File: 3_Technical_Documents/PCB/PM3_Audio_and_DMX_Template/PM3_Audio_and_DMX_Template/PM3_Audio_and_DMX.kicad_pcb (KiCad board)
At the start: 4 copper layers, 66 x 121.9 mm, 187 parts, among them J1 DMX-out, J2 LINE_IN, J3 HEADPHONE_JACK, J4 LINE_OUT, P1 Conn_02x32_Odd_Even, P2 Conn_02x32_Odd_Even, SW2 SW_DPDT_x2, SW3 SW_DPDT_x2, U1 ESP32-WROOM-32E, U10 CS4271, U11 OPA2134, U12 OPA2134, U13 OPA2134, U14 TPA6110A2DGN, U2 LT3045xMSE, U3 6N136S, U4 CRE1S0505SC, U5 ST485E, U6 OPA322, U7 TLV61070ADBV, U8 LD3985M33R_SOT23, U8 LT3045xMSE, U9 LT3045xMSE

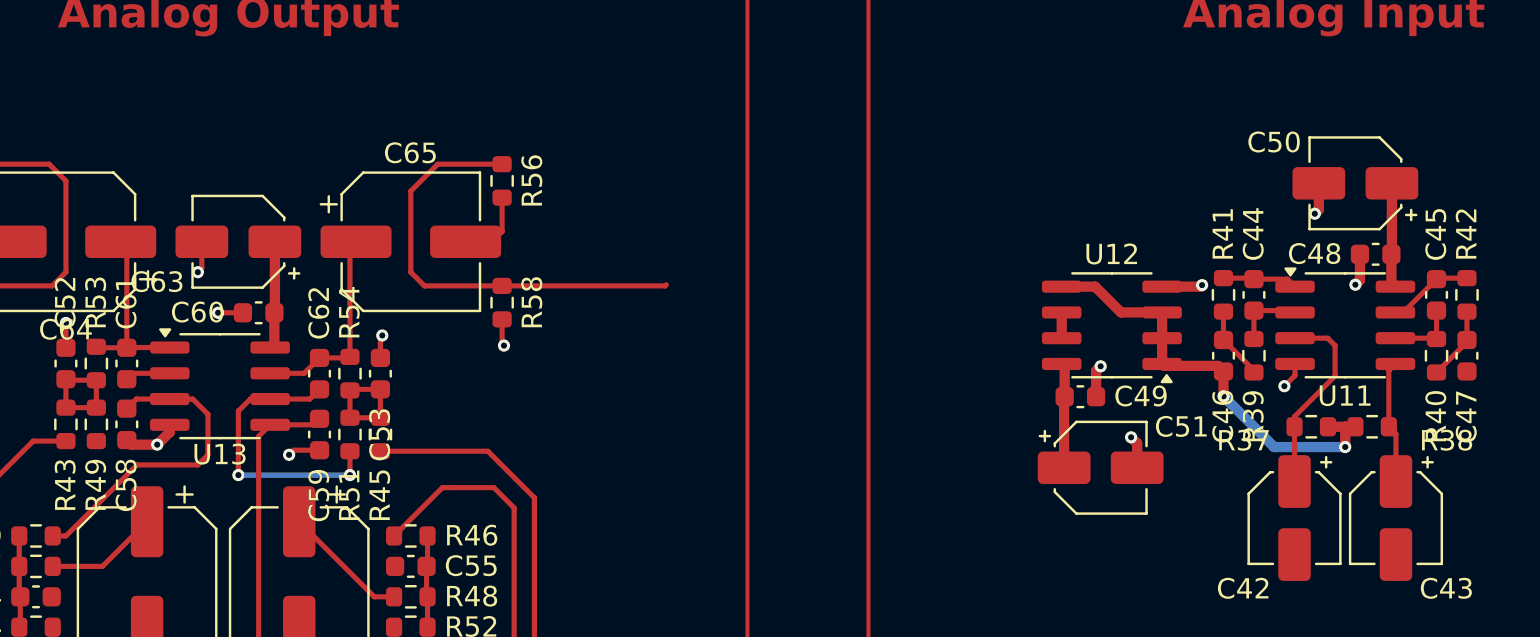
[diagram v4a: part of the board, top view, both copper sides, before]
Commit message: updated capacitors
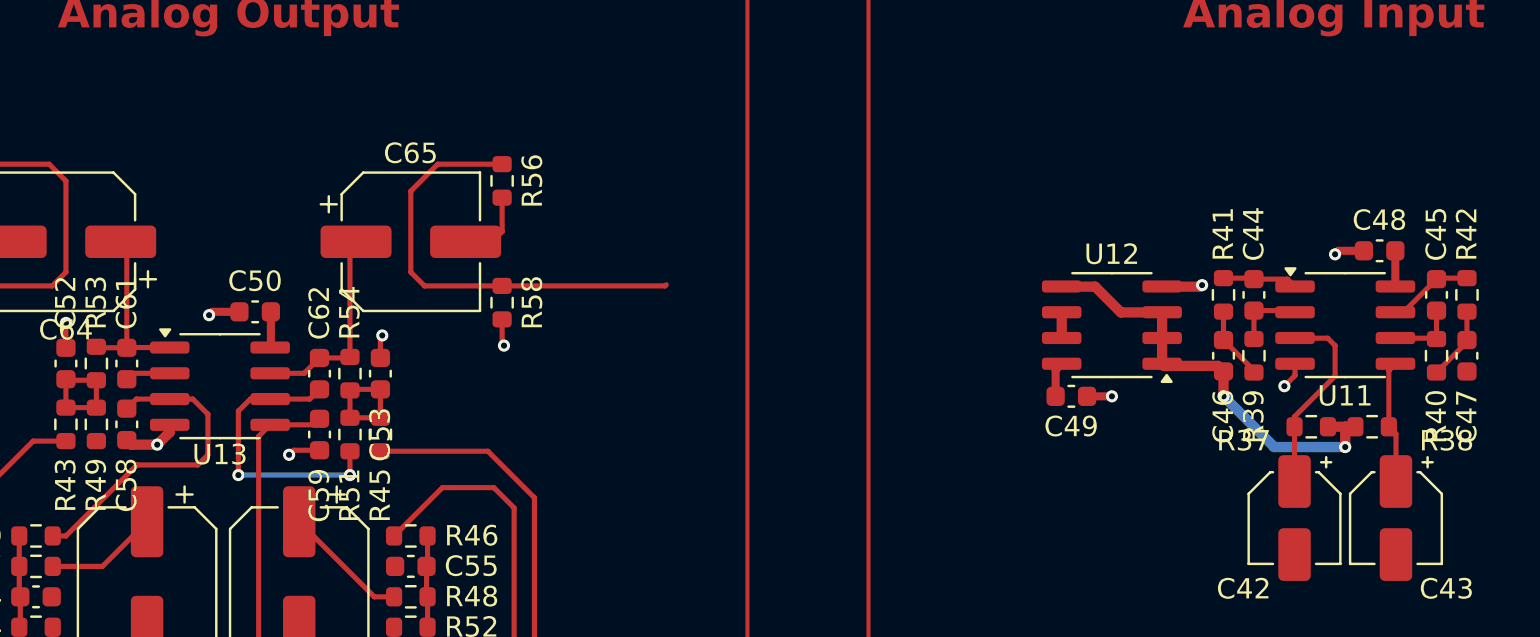
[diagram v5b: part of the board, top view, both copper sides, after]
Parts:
- removed C51, C63: 1u ELEC, Capacitor_SMD:CP_Elec_4x5.8
- removed C60: 10n COG/X7R, Capacitor_SMD:C_0603_1608Metric
- C48, C49: value 10n COG/X7R -> 100n
- C50: value 1u ELEC -> 100n; footprint Capacitor_SMD:CP_Elec_4x5.8 -> Capacitor_SMD:C_0603_1608Metric
- moved C50 54.6 mm to (114.8, -32.7)
- moved C49 0.45 mm to (155.0, -28.5)
- moved C48 0.26 mm to (170.2, -35.7)
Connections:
- R1 pad 2: Net-(U1-IO17) -> Net-(U1-IO16)
- U1 pad 27: unconnected-(U1-IO16-Pad27) -> Net-(U1-IO16)
- U1 pad 28: Net-(U1-IO17) -> unconnected-(U1-IO17-Pad28)
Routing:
- net VA: track 48.2 -> 37.8 mm
- net GND: track 92.5 -> 87.6 mm, vias 85 -> 82

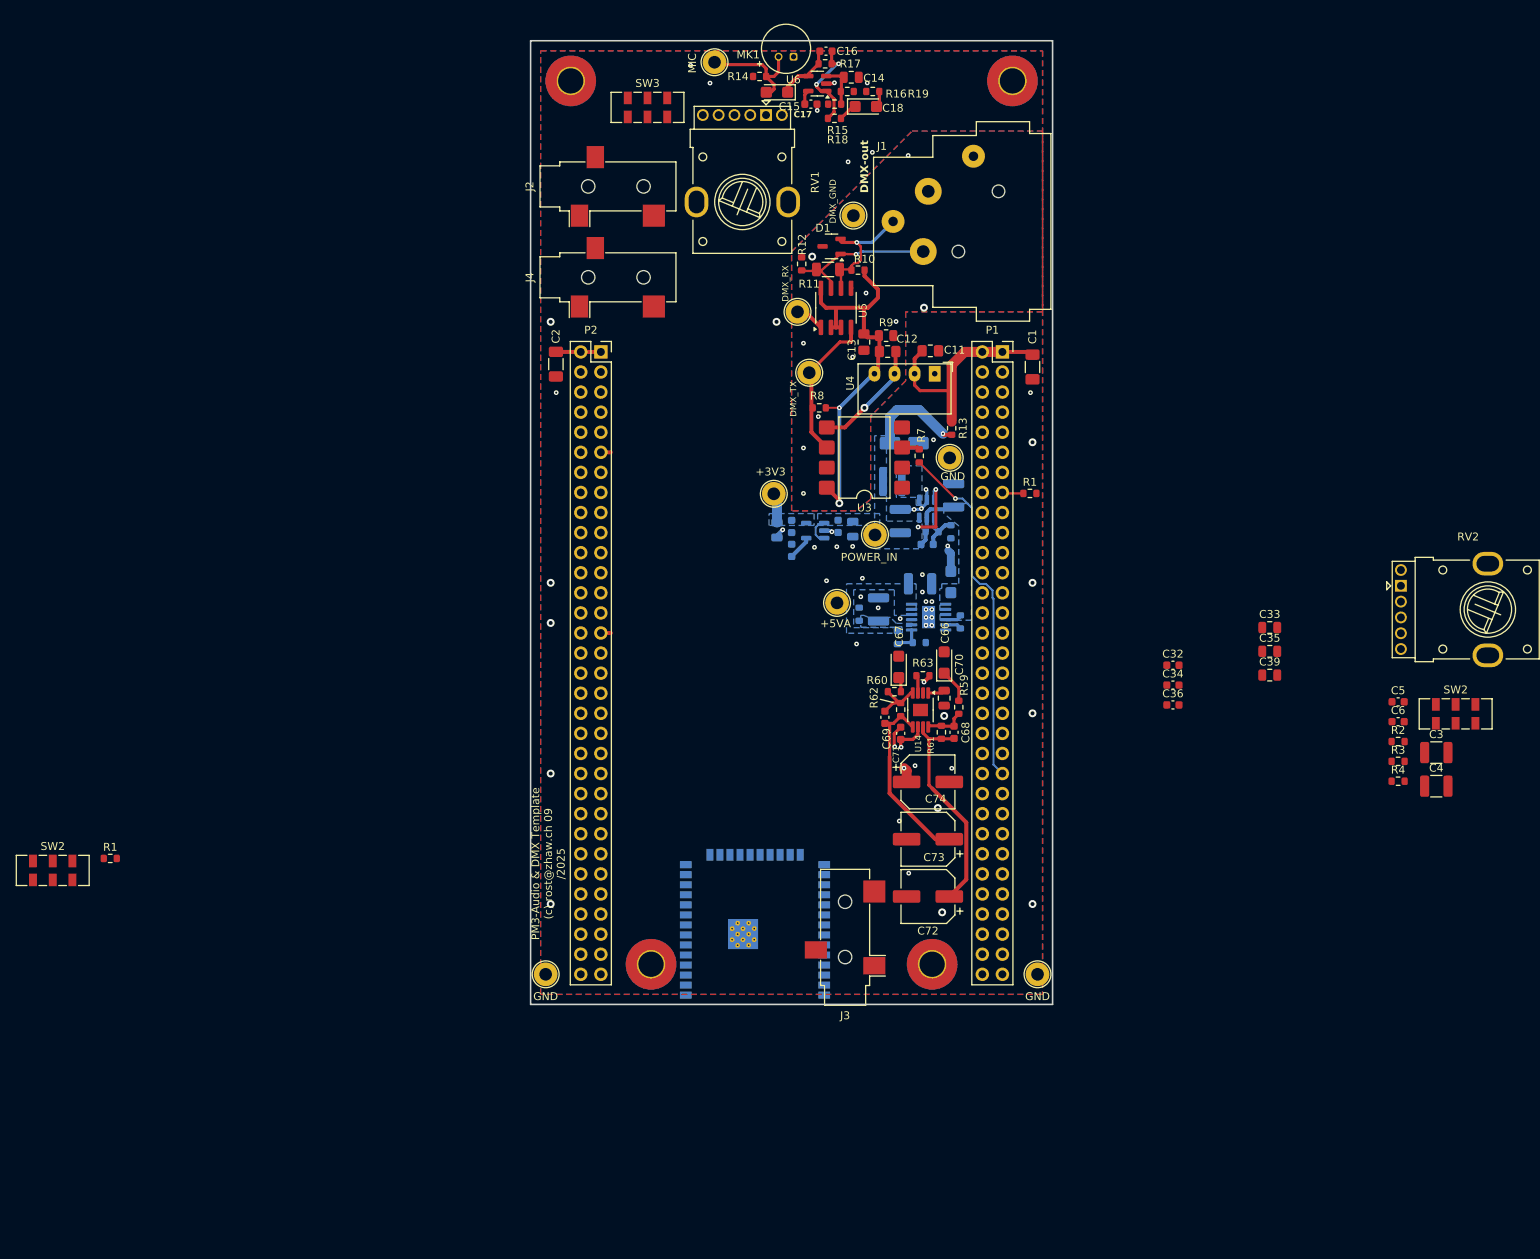
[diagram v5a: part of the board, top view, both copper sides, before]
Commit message: minor modifications to esp32 bootmodes
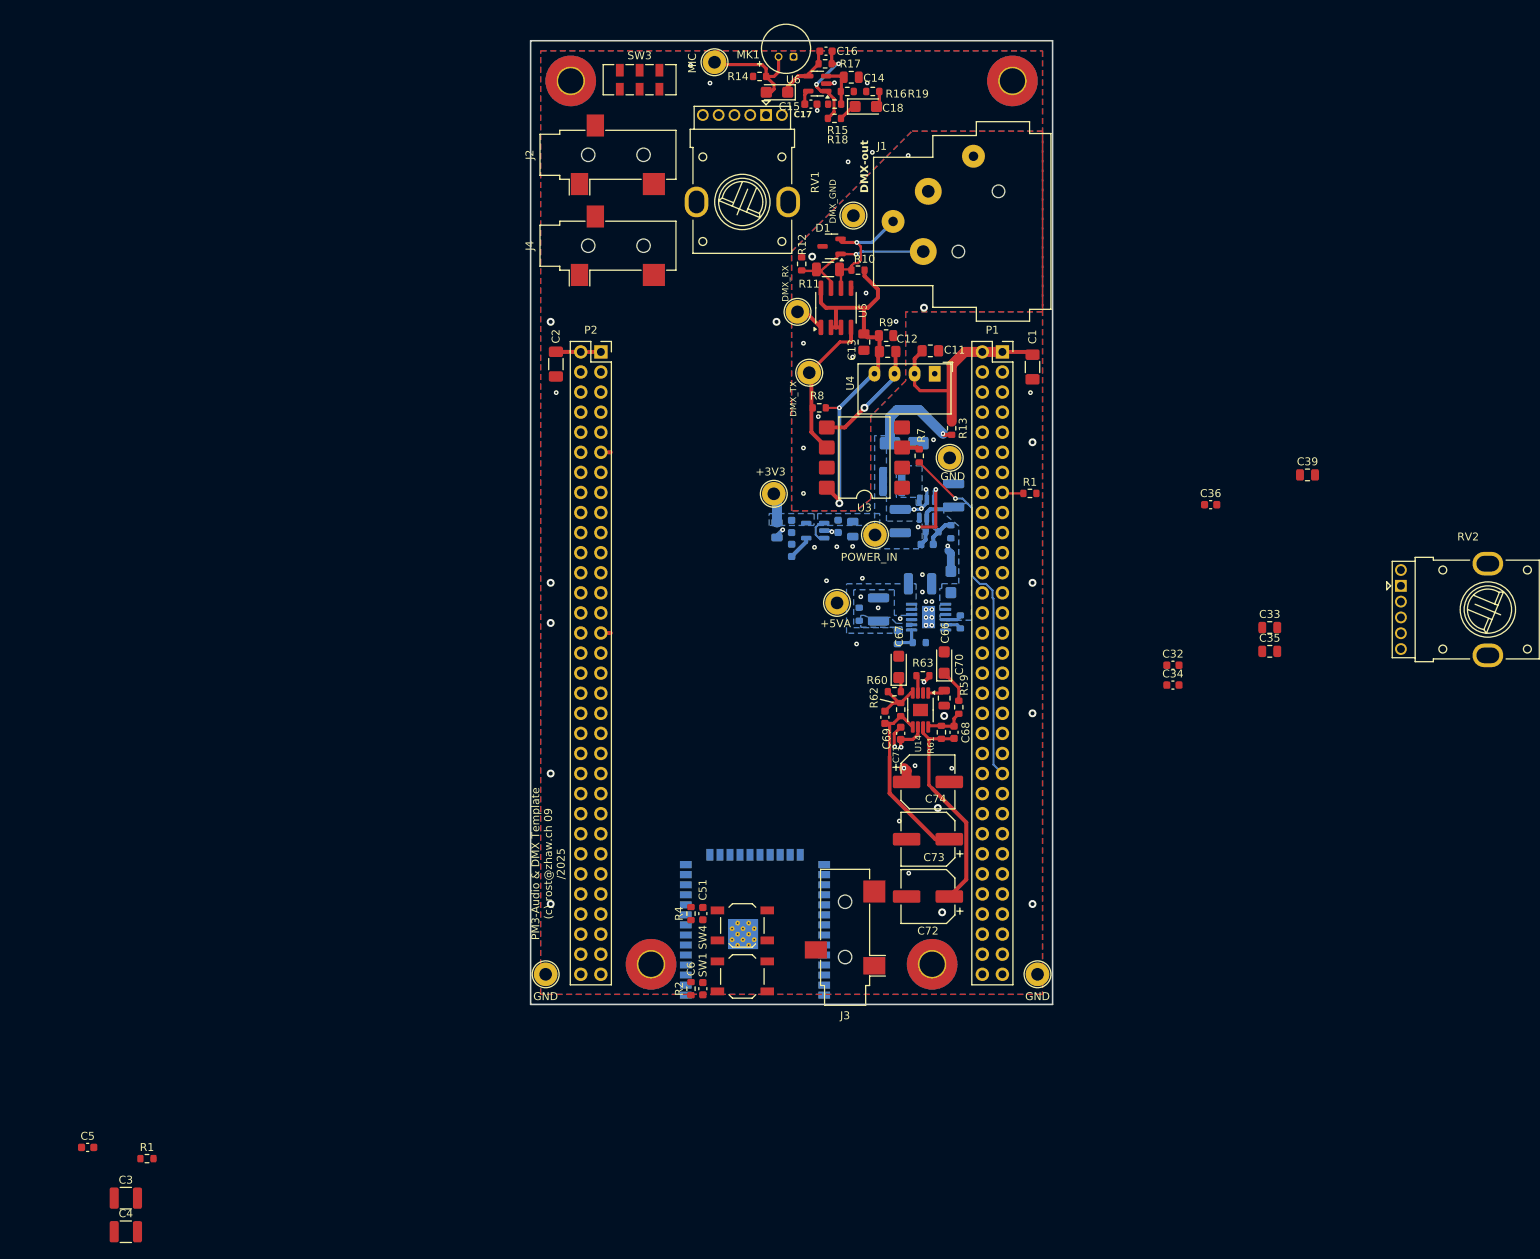
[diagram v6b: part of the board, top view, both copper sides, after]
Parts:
- removed R3: 10k, Resistor_SMD:R_0603_1608Metric
- removed SW2 (x2): SW_DPDT_x2, Button_Switch_SMD:SW_DPDT_CK_JS202011JCQN
- added C51: 100n, Capacitor_SMD:C_0603_1608Metric, F.Cu at (116.0, 140.0)
- added SW1: SW_Push, Button_Switch_SMD:SW_SPST_TL3342, F.Cu at (121.0, 147.9)
- added SW4: SW_Push, Button_Switch_SMD:SW_SPST_TL3342, F.Cu at (121.0, 141.5)
- moved C5 175.1 mm to (38.2, 169.6)
- moved C3 175.1 mm to (43.0, 176.0)
- moved C4 175.1 mm to (43.0, 180.2)
- moved R2 94.8 mm to (114.5, 149.5), turned to 90 degrees
- moved C6 94.2 mm to (116.0, 149.5), turned to 90 degrees
- moved R4 91.0 mm to (114.5, 140.0), turned to -90 degrees
- moved R1 38.3 mm to (45.7, 171.0)
- moved C36 25.8 mm to (180.2, 88.3)
- moved C39 25.8 mm to (192.5, 84.5)
- moved J2 4.00 mm to (104.0, 44.0)
- moved J4 4.00 mm to (104.0, 55.5)
- moved SW3 3.64 mm to (108.0, 34.5)
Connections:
- R4 pad 1: BOOT2 -> BOOT
- R4 pad 2: Net-(SW2B-B) -> +3V3_ESP
- U1 pad 24: unconnected-(U1-IO2-Pad24) -> BOOT

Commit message: esp-stm connection (+ conflict recolution)
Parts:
- removed the C25 at (133.1, 91.0)
- removed the C26 at (135.0, 91.4)
- removed the C27 at (127.2, 94.0)
- removed the C28 at (125.4, 91.5)
- removed the C29 at (127.2, 91.0)
- removed C51: 100n, Capacitor_SMD:C_0603_1608Metric
- removed the R1 at (157.4, 86.8)
- removed SW4: SW_Push, Button_Switch_SMD:SW_SPST_TL3342
- removed the U8 at (130.2, 91.5)
- added C60: 100n, Capacitor_SMD:C_0603_1608Metric, F.Cu at (115.0, -32.5)
- added JP1: SolderJumper_2_Open, Jumper:SolderJumper-2_P1.3mm_Open_RoundedPad1.0x1.5mm, F.Cu at (42.4, 111.8)
- added JP10: SolderJumper_2_Open, Jumper:SolderJumper-2_P1.3mm_Open_RoundedPad1.0x1.5mm, F.Cu at (202.0, -23.5)
- added JP11: SolderJumper_2_Open, Jumper:SolderJumper-2_P1.3mm_Open_RoundedPad1.0x1.5mm, F.Cu at (203.8, 78.0)
- added JP12: SolderJumper_2_Open, Jumper:SolderJumper-2_P1.3mm_Open_RoundedPad1.0x1.5mm, F.Cu at (203.7, 81.5)
- added JP2: SolderJumper_2_Open, Jumper:SolderJumper-2_P1.3mm_Open_RoundedPad1.0x1.5mm, F.Cu at (42.4, 115.4)
- added JP3: SolderJumper_2_Open, Jumper:SolderJumper-2_P1.3mm_Open_RoundedPad1.0x1.5mm, F.Cu at (42.4, 119.0)
- added JP4: SolderJumper_2_Open, Jumper:SolderJumper-2_P1.3mm_Open_RoundedPad1.0x1.5mm, F.Cu at (42.4, 122.5)
- added JP5: SolderJumper_2_Open, Jumper:SolderJumper-2_P1.3mm_Open_RoundedPad1.0x1.5mm, F.Cu at (257.0, -49.0)
- added JP6: SolderJumper_2_Open, Jumper:SolderJumper-2_P1.3mm_Open_RoundedPad1.0x1.5mm, F.Cu at (203.8, -28.5)
- added JP7: SolderJumper_2_Open, Jumper:SolderJumper-2_P1.3mm_Open_RoundedPad1.0x1.5mm, F.Cu at (201.8, -18.2)
- added JP8: SolderJumper_2_Open, Jumper:SolderJumper-2_P1.3mm_Open_RoundedPad1.0x1.5mm, F.Cu at (202.0, -20.9)
- added JP9: SolderJumper_2_Open, Jumper:SolderJumper-2_P1.3mm_Open_RoundedPad1.0x1.5mm, F.Cu at (202.0, -26.0)
- added R3: 10k, Resistor_SMD:R_0603_1608Metric, F.Cu at (114.8, 140.1)
- added SW2: SW_Push, Button_Switch_SMD:SW_SPST_TL3342, F.Cu at (121.3, 141.6)
- moved R4 181.4 mm to (208.5, -15.2), turned to 90 degrees
- moved C50 172.8 mm to (116.3, 140.1), turned to -90 degrees
- moved R1 30.7 mm to (42.5, 140.5)
- moved C3 28.6 mm to (41.0, 147.5)
- moved C4 28.6 mm to (41.0, 151.8)
- moved C5 28.6 mm to (36.1, 141.1)
- moved C36 25.8 mm to (175.5, 113.6)
- moved C39 25.8 mm to (187.7, 109.8)
- moved C49 16.5 mm to (170.0, -35.6), turned to 180 degrees
- moved C48 16.4 mm to (155.4, -28.5), turned to 0 degrees
- moved J2 4.00 mm to (104.0, 48.0)
- moved J4 4.00 mm to (104.0, 59.5)
- moved SW3 3.64 mm to (109.0, 38.0)
- moved C30 1.00 mm to (207.2, -28.5)
- moved C31 1.00 mm to (210.2, -28.5)
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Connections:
- C50 pad 1: VA -> BOOT
- R4 pad 1: BOOT -> VL
- R4 pad 2: +3V3_ESP -> Net-(U10-AD0/~{CS}(I2S/~{LJ}))
- U1 pad 10: LRCLK -> LRCLK_1
- U1 pad 11: BCLK -> BCLK_1
- U1 pad 12: unconnected-(U1-IO27-Pad12) -> PE7_
- U1 pad 24: BOOT -> unconnected-(U1-IO2-Pad24)
- U1 pad 25: MCLK -> BOOT
- U1 pad 28: unconnected-(U1-IO17-Pad28) -> MCLK_ESP
- U1 pad 30: unconnected-(U1-IO18-Pad30) -> LRCLK_2
- U1 pad 31: unconnected-(U1-IO19-Pad31) -> BCLK_2
- U1 pad 33: unconnected-(U1-IO21-Pad33) -> PE8_
- U1 pad 36: DOUT -> DOUT_1
- U1 pad 37: DIN -> DIN_1
- U1 pad 8: unconnected-(U1-IO32-Pad8) -> DOUT_2
- U1 pad 9: unconnected-(U1-IO33-Pad9) -> DIN_2
- U10 pad 13: GND -> Net-(U10-AD0/~{CS}(I2S/~{LJ}))
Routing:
- net VL: track 37.3 -> 47.7 mm, vias 3 -> 4
- net PE6: track 2.84 -> 7.31 mm
- net Net-(U10-AD0/~{CS}(I2S/~{LJ})): track 0.00 -> 4.35 mm
- net VD: track 0.00 -> 3.23 mm
- net +3.3V: track 3.23 -> 0.00 mm
- net Net-(U8-BYP): track 3.08 -> 0.00 mm
- net (no net): track 0.00 -> 3.08 mm
- net PE3: track 0.00 -> 2.67 mm
- net GND: track 87.6 -> 85.0 mm, vias 82 -> 81
- net /ESP32/Digital Power Supply/+5V: track 18.6 -> 20.9 mm
- net PE4: track 0.00 -> 2.28 mm
- net PE5: track 0.00 -> 2.17 mm
- net PE2: track 2.23 -> 4.27 mm
- net Net-(U10-SDIN): track 3.20 -> 4.47 mm

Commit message: layout complete
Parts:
- C10, C26, C27, C28, C29, C42, C43, C44, C45, C46, C47, C48, C49, C7, C8, C9, JP1, JP11, JP12, JP2, JP3, JP4, JP5, R26, R27, R37, R38, R39, R40, R41, R42, R5, R6, U11, U12, U2, U9: moved to B.Cu
- moved C10 228.7 mm to (111.5, 123.7)
- moved C9 223.3 mm to (116.0, 120.2), turned to -90 degrees
- moved U2 222.5 mm to (110.8, 119.7)
- moved R5 222.5 mm to (118.5, 119.7), turned to -90 degrees
- moved R6 221.7 mm to (106.5, 119.2), turned to 90 degrees
- moved JP5 217.5 mm to (115.8, 116.4)
- moved C8 215.6 mm to (113.0, 115.2), turned to 90 degrees
- moved C7 214.9 mm to (111.0, 114.7), turned to 90 degrees
- moved C41 193.7 mm to (110.0, 130.5), turned to 180 degrees
- moved Y1 186.5 mm to (121.8, 133.5), turned to 0 degrees
- moved C29 183.4 mm to (112.4, 88.3)
- moved C31 182.7 mm to (120.3, 130.5), turned to 180 degrees
- moved C30 179.8 mm to (123.3, 130.5), turned to 0 degrees
- moved C28 179.2 mm to (116.9, 84.9), turned to -90 degrees
- moved C38 178.6 mm to (113.8, 124.0), turned to -90 degrees
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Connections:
- U1 pad 36: DOUT_1 -> DIN_1
- U1 pad 37: DIN_1 -> DOUT_1
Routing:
- net GND: track 85.0 -> 691.8 mm, vias 81 -> 37
- net VA: track 37.8 -> 221.0 mm, vias 2 -> 7
- net PE4: track 2.28 -> 111.7 mm, vias 0 -> 3
- net PE5: track 2.17 -> 107.4 mm, vias 0 -> 3
- net /PM3 Audio/Codec with analog line buffers/Audio Input/AINA: track 3.62 -> 99.9 mm, vias 0 -> 2
- net /PM3 Audio/Codec with analog line buffers/Audio Input/AINB: track 3.62 -> 98.9 mm, vias 0 -> 2
- net VCOM: track 31.0 -> 121.6 mm, vias 2 -> 5
- net +5V: track 27.4 -> 113.5 mm, vias 0 -> 1
- net VL: track 47.7 -> 132.7 mm, vias 4 -> 6
- net PE6: track 7.31 -> 79.6 mm, vias 0 -> 1
- net PE2: track 4.27 -> 69.4 mm
- net /PM3 Audio/Codec with analog line buffers/LINE_OUT_R: track 21.9 -> 86.1 mm, vias 0 -> 2
- net /PM3 Audio/Codec with analog line buffers/LINE_OUT_L: track 24.9 -> 86.0 mm, vias 0 -> 3
- net /PM3 Audio/Headphone Amplifier/in_r: track 0.00 -> 59.6 mm, vias 0 -> 1
- net /PM3 Audio/Headphone Amplifier/in_l: track 0.00 -> 54.6 mm, vias 0 -> 1
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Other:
- board text removed: "Analog Input"
- board text removed: "Analog Output"
- board text removed: "Codec"
- board text removed: "ESP32 +3V3 Power"
- board text removed: "PM3 +3V3 Power"
